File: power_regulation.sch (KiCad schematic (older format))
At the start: 6 parts

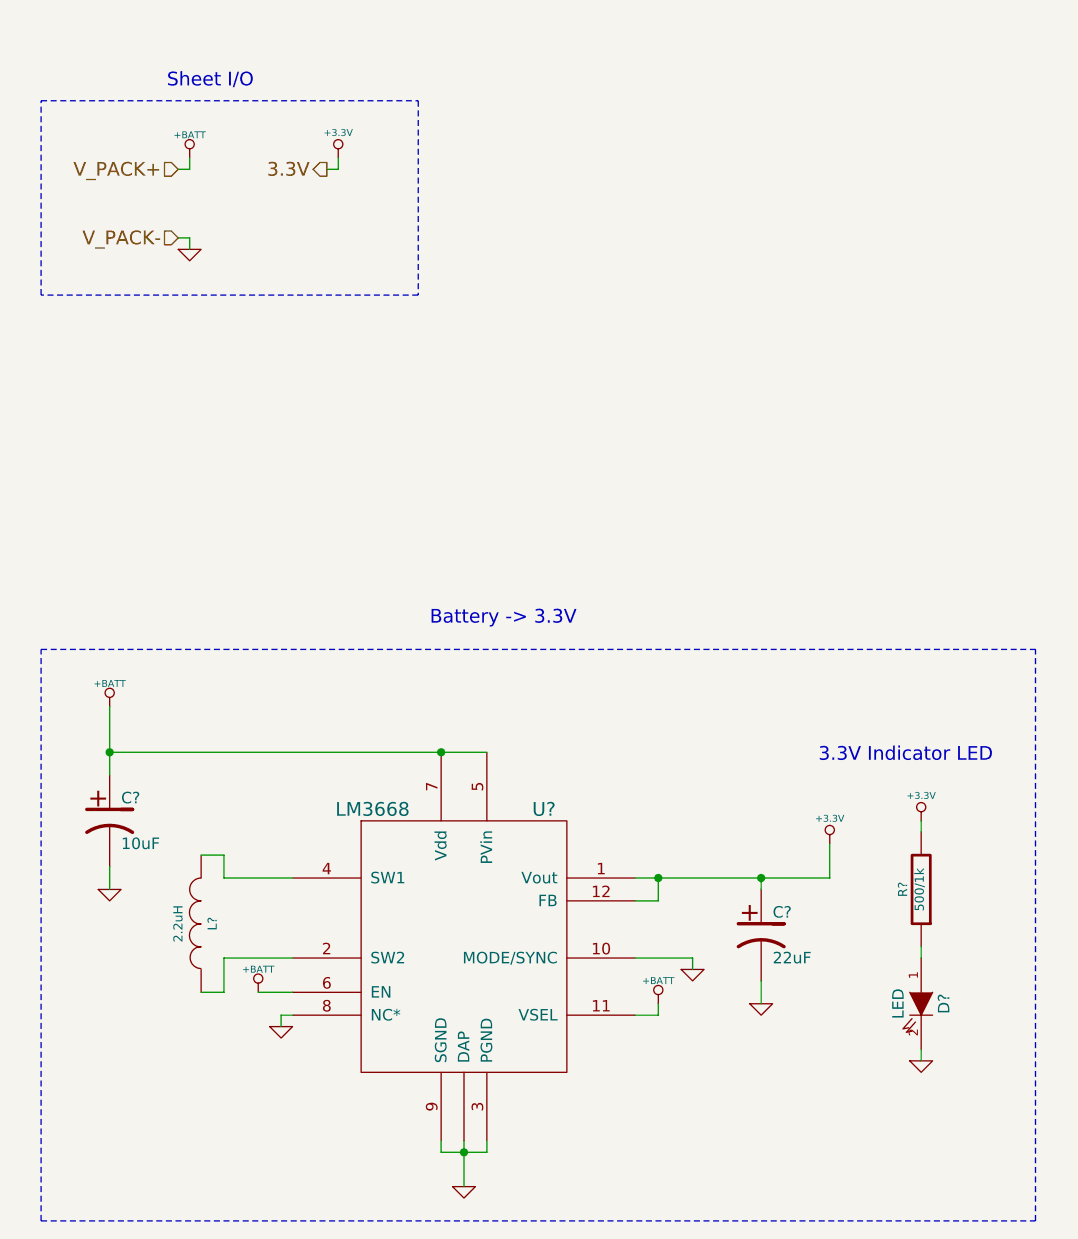
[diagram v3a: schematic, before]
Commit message: general organization, fixed power reg sheet, added jtag
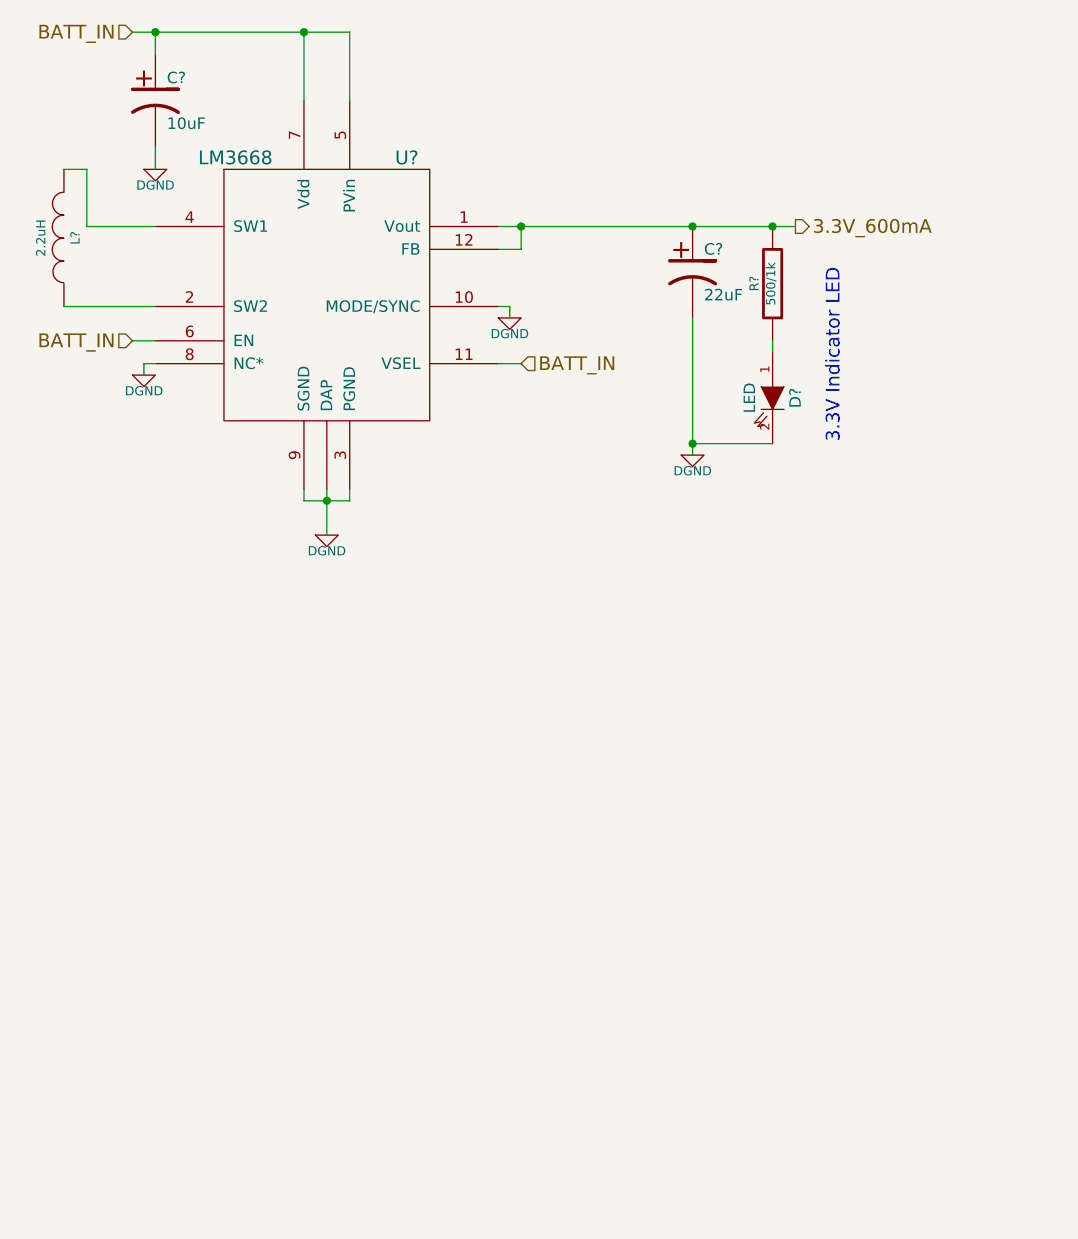
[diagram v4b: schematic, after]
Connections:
- net +3.3V renamed 3.3V_600mA
- net +BATT renamed BATT_IN
- net GND renamed DGND
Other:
- note removed: "Battery -> 3.3V"
- note removed: "Sheet I/O"
- moved on the sheet: C?, D?, L?, R?, U?
